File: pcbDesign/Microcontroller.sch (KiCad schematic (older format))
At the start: 7 parts

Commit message: Cerrected errors in the schematic and began work on the pcb layout
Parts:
- added C7: 500n, Capacitor_SMD:C_0402_1005Metric, symbol Device:C
- gave numbers to parts that had none: 7
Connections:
- net GND: now also C7.1
- net VBUS_3V3_CH0_REG: now also C7.2
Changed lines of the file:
@@
 $EndDescr
 $Comp
-L power:GND #PWR?
+L power:GND #PWR09
 U 1 1 6044DE61
 P 5300 5700
-F 0 "#PWR?" H 5300 5450 50  0001 C CNN
+F 0 "#PWR09" H 5300 5450 50  0001 C CNN
 F 1 "GND" H 5305 5527 50  0000 C CNN
 F 2 "" H 5300 5700 50  0001 C CNN
@@
 $EndComp
 $Comp
-L Device:R R?
+L Device:R R3
 U 1 1 6044DE67
 P 4400 5800
-F 0 "R?" V 4193 5800 50  0000 C CNN
+F 0 "R3" V 4193 5800 50  0000 C CNN
 F 1 "10K" V 4284 5800 50  0000 C CNN
 F 2 "Resistor_SMD:R_0402_1005Metric" V 4330 5800 50  0001 C CNN
@@
 P 4250 5450
 AR Path="/604550E7" Ref="C?"  Part="1"
-AR Path="/604479FD/604550E7" Ref="C?"  Part="1"
-F 0 "C?" H 4135 5404 50  0000 R CNN
+AR Path="/604479FD/604550E7" Ref="C5"  Part="1"
+F 0 "C5" H 4135 5404 50  0000 R CNN
 F 1 "1u" H 4135 5495 50  0000 R CNN
 F 2 "Capacitor_SMD:C_0402_1005Metric" H 4288 5300 50  0001 C CNN
@@
 $EndComp
 $Comp
-L power:GND #PWR?
+L power:GND #PWR07
 U 1 1 6045514C
 P 4100 5450
-F 0 "#PWR?" H 4100 5200 50  0001 C CNN
+F 0 "#PWR07" H 4100 5200 50  0001 C CNN
 F 1 "GND" H 4105 5277 50  0000 C CNN
 F 2 "" H 4100 5450 50  0001 C CNN
@@
 P 5300 3800
 AR Path="/6044DE5A" Ref="U?"  Part="1"
-AR Path="/604479FD/6044DE5A" Ref="U?"  Part="1"
-F 0 "U?" H 5300 1811 50  0001 C CNN
+AR Path="/604479FD/6044DE5A" Ref="U2"  Part="1"
+F 0 "U2" H 5300 1811 50  0001 C CNN
 F 1 "ATSAME51J18A-A" H 5300 1720 50  0000 C CNN
 F 2 "Package_QFP:TQFP-64_10x10mm_P0.5mm" H 6600 5700 50  0001 C CNN
@@
 P 5000 1750
 AR Path="/604A4817" Ref="C?"  Part="1"
-AR Path="/604479FD/604A4817" Ref="C?"  Part="1"
-F 0 "C?" H 4885 1704 50  0000 R CNN
+AR Path="/604479FD/604A4817" Ref="C6"  Part="1"
+F 0 "C6" H 4885 1704 50  0000 R CNN
 F 1 "1u" H 4885 1795 50  0000 R CNN
 F 2 "Capacitor_SMD:C_0402_1005Metric" H 5038 1600 50  0001 C CNN
@@
 $EndComp
 $Comp
-L power:GND #PWR?
+L power:GND #PWR08
 U 1 1 604A6978
 P 5000 1600
-F 0 "#PWR?" H 5000 1350 50  0001 C CNN
+F 0 "#PWR08" H 5000 1350 50  0001 C CNN
 F 1 "GND" H 5005 1427 50  0000 C CNN
 F 2 "" H 5000 1600 50  0001 C CNN
@@
 31
 $Comp
-L Device:Crystal Y?
+L Device:Crystal Y1
 U 1 1 604B1962
 P 3700 1950
-F 0 "Y?" H 3700 2218 50  0000 C CNN
+F 0 "Y1" H 3700 2218 50  0000 C CNN
 F 1 "32.768" H 3700 2127 50  0000 C CNN
 F 2 "Oscillator:Oscillator_SMD_Abracon_ASCO-4Pin_1.6x1.2mm" H 3700 1950 50  0001 C CNN
@@
 P 4000 1950
 AR Path="/604B399F" Ref="C?"  Part="1"
-AR Path="/604479FD/604B399F" Ref="C?"  Part="1"
-F 0 "C?" H 3885 1904 50  0000 R CNN
+AR Path="/604479FD/604B399F" Ref="C4"  Part="1"
+F 0 "C4" H 3885 1904 50  0000 R CNN
 F 1 "22u" H 3885 1995 50  0000 R CNN
 F 2 "Capacitor_SMD:C_0402_1005Metric" H 4038 1800 50  0001 C CNN
@@
 P 3400 1950
 AR Path="/604B6163" Ref="C?"  Part="1"
-AR Path="/604479FD/604B6163" Ref="C?"  Part="1"
-F 0 "C?" H 3285 1904 50  0000 R CNN
+AR Path="/604479FD/604B6163" Ref="C3"  Part="1"
+F 0 "C3" H 3285 1904 50  0000 R CNN
 F 1 "22u" H 3285 1995 50  0000 R CNN
 F 2 "Capacitor_SMD:C_0402_1005Metric" H 3438 1800 50  0001 C CNN
@@
 	3250 1600 3250 1950
 $Comp
-L power:GND #PWR?
+L power:GND #PWR06
 U 1 1 604B7059
 P 3700 1600
-F 0 "#PWR?" H 3700 1350 50  0001 C CNN
+F 0 "#PWR06" H 3700 1350 50  0001 C CNN
 F 1 "GND" H 3705 1427 50  0000 C CNN
 F 2 "" H 3700 1600 50  0001 C CNN
@@
 Text GLabel 4400 5000 0    50   BiDi ~ 0
 CAN_S
+$Comp
+L Device:C C?
+U 1 1 606356DA
+P 5500 1750
+AR Path="/606356DA" Ref="C?"  Part="1"
+AR Path="/604479FD/606356DA" Ref="C7"  Part="1"
+F 0 "C7" H 5385 1704 50  0000 R CNN
+F 1 "500n" H 5385 1795 50  0000 R CNN
+F 2 "Capacitor_SMD:C_0402_1005Metric" H 5538 1600 50  0001 C CNN
+F 3 "~" H 5500 1750 50  0001 C CNN
+	1    5500 1750
+	1    0    0    -1
+$EndComp
+$Comp
+L power:GND #PWR010
+U 1 1 6063675F
+P 5500 1600
+F 0 "#PWR010" H 5500 1350 50  0001 C CNN
+F 1 "GND" H 5505 1427 50  0000 C CNN
+F 2 "" H 5500 1600 50  0001 C CNN
+F 3 "" H 5500 1600 50  0001 C CNN
+	1    5500 1600
+	-1   0    0    1
+$EndComp
 $EndSCHEMATC

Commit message: Finnished routing
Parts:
- Y1: footprint Oscillator:Oscillator_SMD_Abracon_ASCO-4Pin_1.6x1.2mm -> Crystal:Crystal_SMD_2012-2Pin_2.0x1.2mm
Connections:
- net LED_PIN is gone; now on net 13: U2.60 (PB31/I15/S5.0/P0.1)
- net 13: no longer U2.26 (PB13/I13/S4.1/I2SMCK1/SD0WP/T27/P4.1/CRX1)
- net 15[I2SFS] renamed 7[I2SWS]
- net 6[I2SCK] renamed 6[I2SSCK]
- net USB_DM renamed USB_N
- net USB_DP renamed USB_P
- new net 15: U2.26 (PB13/I13/S4.1/I2SMCK1/SD0WP/T27/P4.1/CRX1)
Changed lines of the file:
@@
 $EndComp
 Text GLabel 4400 4800 0    50   BiDi ~ 0
-USB_DM
+USB_N
 Text GLabel 4400 4900 0    50   BiDi ~ 0
-USB_DP
+USB_P
 Wire Wire Line
 	4400 5400 4400 5450
@@
 AREF
 Text GLabel 8500 4000 2    50   BiDi ~ 0
-6[I2SCK]
+6[I2SSCK]
 Text GLabel 8500 4100 2    50   BiDi ~ 0
 14[I2SMCLK]
@@
 10[I2SDO]
 Text GLabel 4400 4400 0    50   BiDi ~ 0
-15[I2SFS]
+7[I2SWS]
 Text GLabel 3950 5650 0    50   BiDi ~ 0
 RST
@@
 Text GLabel 8500 3600 2    50   BiDi ~ 0
 12
-Text GLabel 8500 3700 2    50   BiDi ~ 0
+Text GLabel 8500 4600 3    50   BiDi ~ 0
 13
 Text GLabel 4400 2800 0    50   BiDi ~ 0
@@
 F 0 "Y1" H 3700 2218 50  0000 C CNN
 F 1 "32.768" H 3700 2127 50  0000 C CNN
-F 2 "Oscillator:Oscillator_SMD_Abracon_ASCO-4Pin_1.6x1.2mm" H 3700 1950 50  0001 C CNN
+F 2 "Crystal:Crystal_SMD_2012-2Pin_2.0x1.2mm" H 3700 1950 50  0001 C CNN
 F 3 "~" H 3700 1950 50  0001 C CNN
 	1    3700 1950
@@
 	-1   0    0    1
 $EndComp
+Wire Wire Line
+	8500 4600 8500 4500
+Text GLabel 8500 3700 2    50   BiDi ~ 0
+15
 $EndSCHEMATC

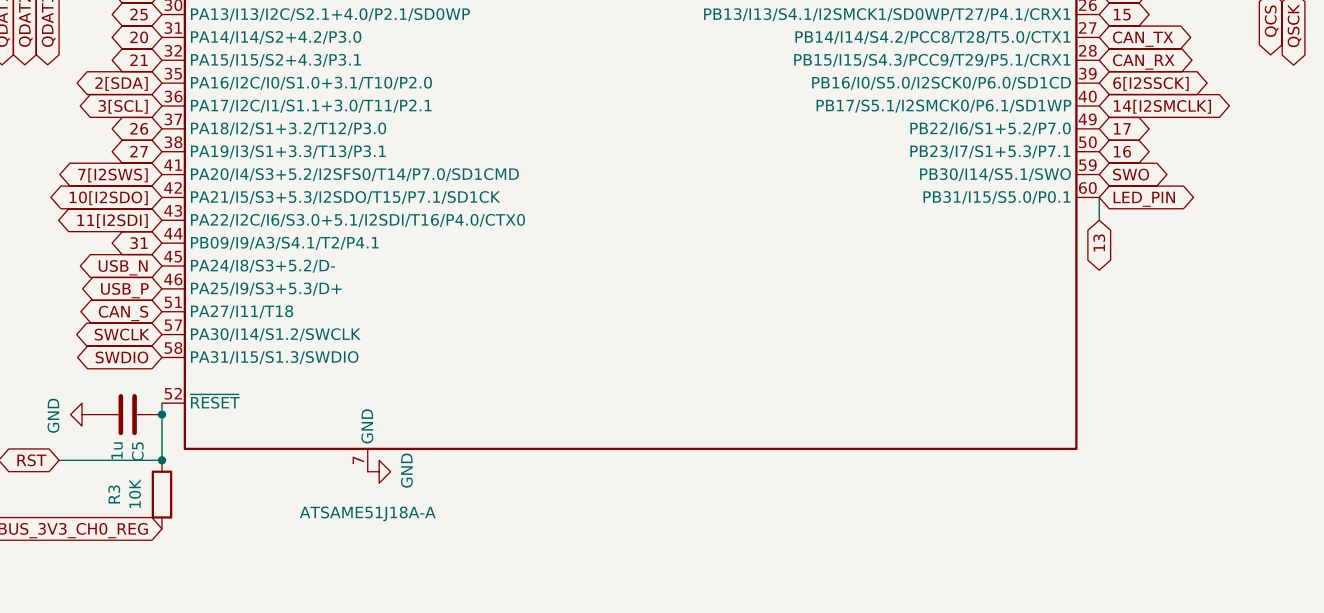
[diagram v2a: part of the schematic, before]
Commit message: Changed the layout of pins to make room for SWD and made the board longer
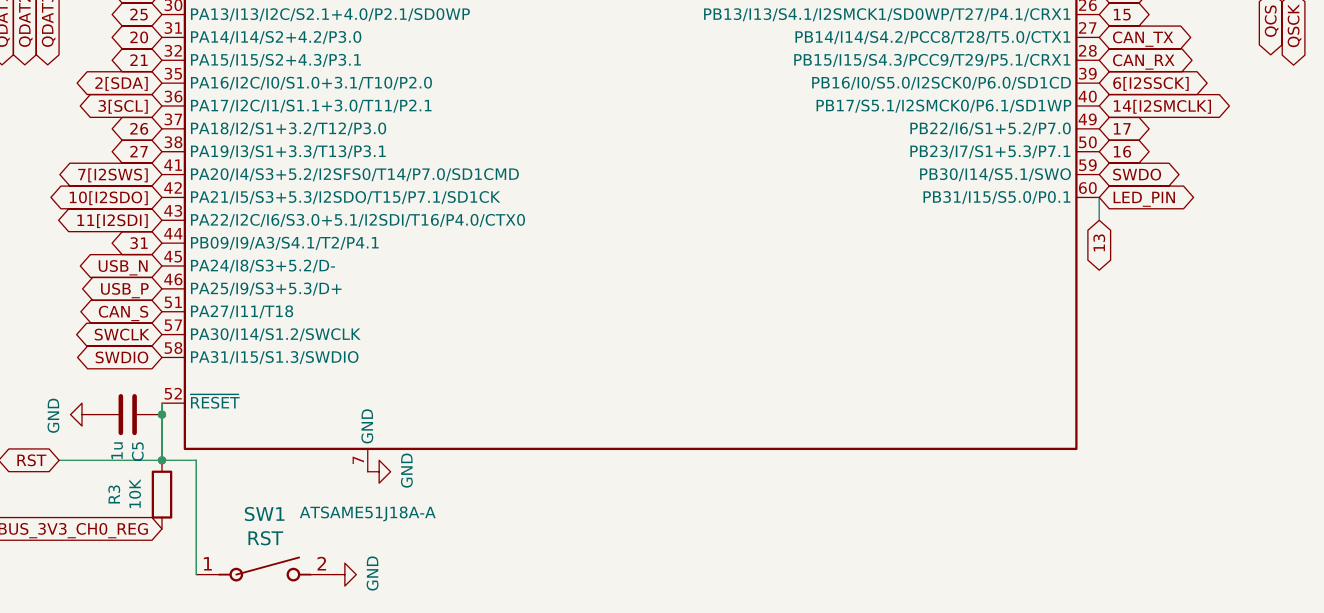
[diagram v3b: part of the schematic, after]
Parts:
- added SW1: RST, PTS636:PTS636 SM25F SMTR LFS, symbol PTS636:PTS636_SM25F_SMTR_LFS
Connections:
- net GND: now also SW1.2
- net RST: now also SW1.1
- net SWO renamed SWDO
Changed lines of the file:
@@
 SWDIO
 Text GLabel 8500 4400 2    50   BiDi ~ 0
-SWO
+SWDO
 Text GLabel 3600 3550 3    50   BiDi ~ 0
 QDAT0
@@
 Text GLabel 8500 3700 2    50   BiDi ~ 0
 15
+Wire Wire Line
+	4400 5650 4550 5650
+Wire Wire Line
+	4550 5650 4550 6150
+$Comp
+L power:GND #PWR0107
+U 1 1 60510F6A
+P 5150 6150
+F 0 "#PWR0107" H 5150 5900 50  0001 C CNN
+F 1 "GND" H 5155 5977 50  0000 C CNN
+F 2 "" H 5150 6150 50  0001 C CNN
+F 3 "" H 5150 6150 50  0001 C CNN
+	1    5150 6150
+	0    -1   -1   0
+$EndComp
+$Comp
+L PTS636:PTS636_SM25F_SMTR_LFS SW1
+U 1 1 60513314
+P 4850 6150
+F 0 "SW1" H 4850 6413 60  0000 C CNN
+F 1 "RST" H 4850 6307 60  0000 C CNN
+F 2 "PTS636:PTS636 SM25F SMTR LFS" H 4850 5965 60  0001 C CNN
+F 3 "" H 4850 6150 60  0000 C CNN
+	1    4850 6150
+	1    0    0    -1
+$EndComp
 $EndSCHEMATC

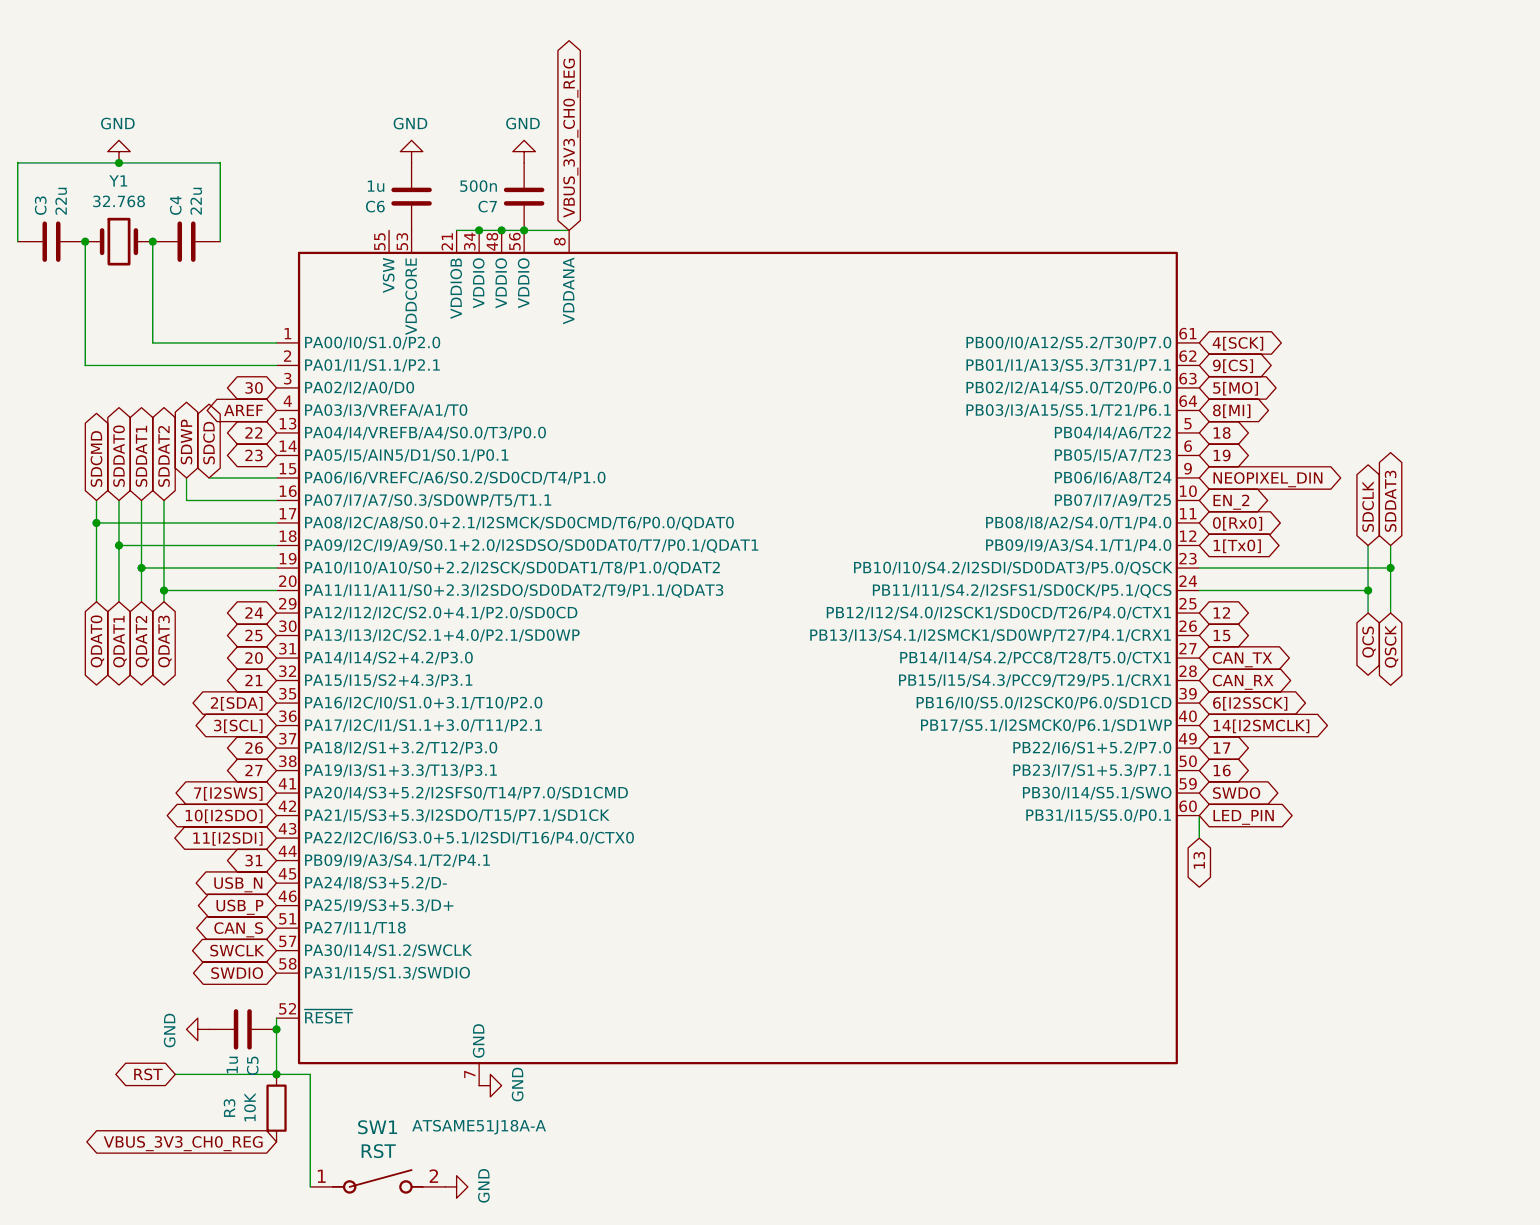
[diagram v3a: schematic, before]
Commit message: Rewired SD card to SPI for ease of use
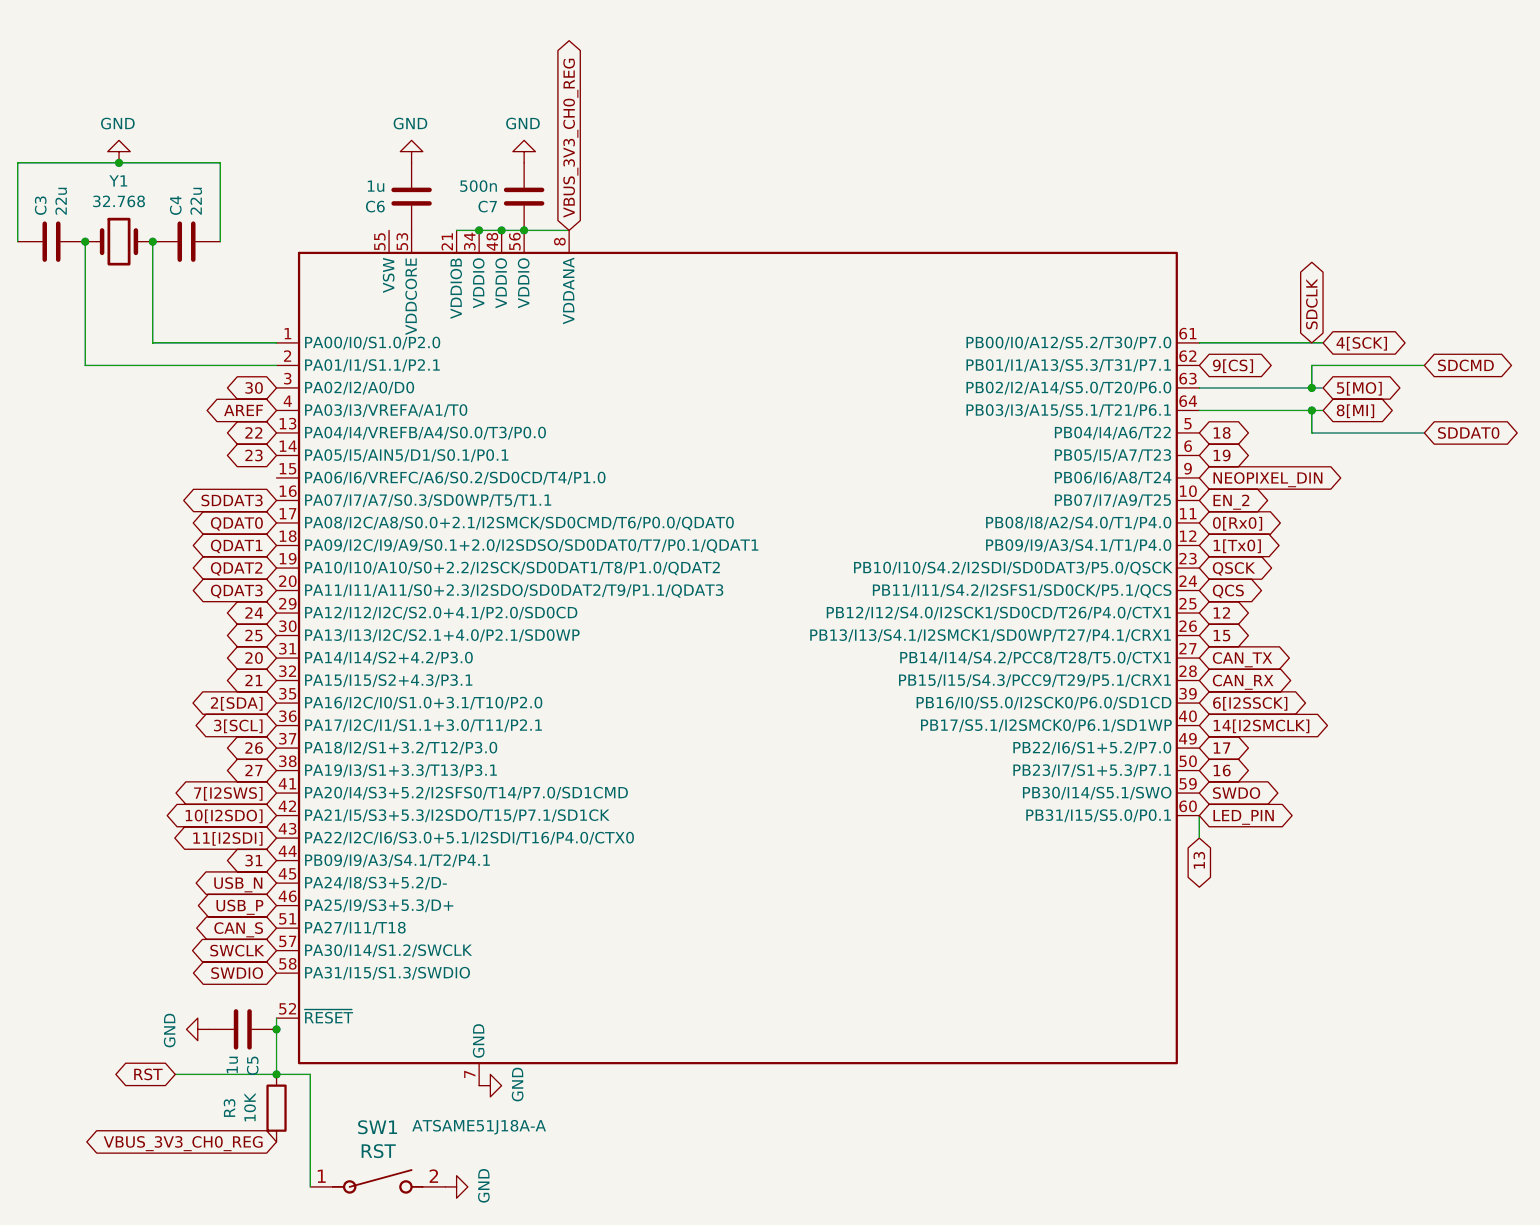
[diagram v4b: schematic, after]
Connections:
- net SDCD: no longer names the net of U2.15 (PA06/I6/VREFC/A6/S0.2/SD0CD/T4/P1.0)
- net SDWP renamed SDDAT3
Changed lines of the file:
@@
 Text GLabel 8500 4400 2    50   BiDi ~ 0
 SWDO
-Text GLabel 3600 3550 3    50   BiDi ~ 0
+Text GLabel 4400 3200 0    50   BiDi ~ 0
 QDAT0
-Text GLabel 3700 3550 3    50   BiDi ~ 0
+Text GLabel 4400 3300 0    50   BiDi ~ 0
 QDAT1
-Text GLabel 3800 3550 3    50   BiDi ~ 0
+Text GLabel 4400 3400 0    50   BiDi ~ 0
 QDAT2
-Text GLabel 3900 3550 3    50   BiDi ~ 0
+Text GLabel 4400 3500 0    50   BiDi ~ 0
 QDAT3
-Text GLabel 9350 3600 3    50   BiDi ~ 0
+Text GLabel 8500 3400 2    50   BiDi ~ 0
 QSCK
-Text GLabel 9250 3600 3    50   BiDi ~ 0
+Text GLabel 8500 3500 2    50   BiDi ~ 0
 QCS
 Text GLabel 4400 4000 0    50   BiDi ~ 0
@@
 	3950 5650 4400 5650
 Connection ~ 4400 5650
-Text GLabel 8500 2400 2    50   BiDi ~ 0
+Text GLabel 9050 2400 2    50   BiDi ~ 0
 4[SCK]
-Text GLabel 8500 2600 2    50   BiDi ~ 0
+Text GLabel 9050 2600 2    50   BiDi ~ 0
 5[MO]
-Text GLabel 8500 2700 2    50   BiDi ~ 0
+Text GLabel 9050 2700 2    50   BiDi ~ 0
 8[MI]
 Text GLabel 8500 2500 2    50   BiDi ~ 0
 9[CS]
-Text GLabel 3600 3100 1    50   BiDi ~ 0
+Text GLabel 9500 2500 2    50   BiDi ~ 0
 SDCMD
-Text GLabel 9350 3300 1    50   BiDi ~ 0
+Text GLabel 4400 3100 0    50   BiDi ~ 0
 SDDAT3
-Text GLabel 3900 3100 1    50   BiDi ~ 0
-SDDAT2
-Text GLabel 9250 3300 1    50   BiDi ~ 0
+Text GLabel 9000 2400 1    50   BiDi ~ 0
 SDCLK
-Text GLabel 3700 3100 1    50   BiDi ~ 0
+Text GLabel 9500 2800 2    50   BiDi ~ 0
 SDDAT0
-Text GLabel 3800 3100 1    50   BiDi ~ 0
-SDDAT1
-Wire Wire Line
-	4400 3500 3900 3500
-Wire Wire Line
-	3900 3500 3900 3550
-Wire Wire Line
-	3800 3400 3800 3550
-Wire Wire Line
-	4400 3300 3700 3300
-Wire Wire Line
-	3700 3300 3700 3550
-Wire Wire Line
-	4400 3200 3600 3200
-Wire Wire Line
-	3600 3200 3600 3550
-Wire Wire Line
-	3600 3100 3600 3200
-Connection ~ 3600 3200
-Wire Wire Line
-	3700 3100 3700 3300
-Connection ~ 3700 3300
-Wire Wire Line
-	4400 3400 3800 3400
-Wire Wire Line
-	3800 3100 3800 3400
-Connection ~ 3800 3400
-Wire Wire Line
-	3900 3100 3900 3500
-Connection ~ 3900 3500
-Wire Wire Line
-	8500 3400 9350 3400
-Wire Wire Line
-	9350 3400 9350 3300
-Wire Wire Line
-	8500 3500 9250 3500
-Wire Wire Line
-	9250 3500 9250 3300
-Wire Wire Line
-	9350 3600 9350 3400
-Connection ~ 9350 3400
-Wire Wire Line
-	9250 3600 9250 3500
-Connection ~ 9250 3500
 Text GLabel 8500 2800 2    50   BiDi ~ 0
 18
@@
 Text GLabel 8500 4500 2    50   BiDi ~ 0
 LED_PIN
-Text GLabel 4100 3000 1    50   BiDi ~ 0
-SDCD
-Text GLabel 4000 3000 1    50   BiDi ~ 0
-SDWP
-Wire Wire Line
-	4100 3000 4400 3000
-Wire Wire Line
-	4400 3100 4000 3100
-Wire Wire Line
-	4000 3100 4000 3000
 Text GLabel 8500 3300 2    50   BiDi ~ 0
 1[Tx0]
@@
 	1    0    0    -1
 $EndComp
+Wire Wire Line
+	8500 2600 9000 2600
+Wire Wire Line
+	9050 2700 9000 2700
+Wire Wire Line
+	8500 2400 9050 2400
+Wire Wire Line
+	9500 2500 9000 2500
+Wire Wire Line
+	9000 2500 9000 2600
+Connection ~ 9000 2600
+Wire Wire Line
+	9000 2600 9050 2600
+Wire Wire Line
+	9500 2800 9000 2800
+Wire Wire Line
+	9000 2800 9000 2700
+Connection ~ 9000 2700
+Wire Wire Line
+	9000 2700 8500 2700
 $EndSCHEMATC

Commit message: Begun to make changes to the design
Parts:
- SW1: symbol PTS636:PTS636_SM25F_SMTR_LFS -> ATSAME51J18A-devboard-rescue:PTS636_SM25F_SMTR_LFS-PTS636
- U2: symbol MCU_Microchip_SAME:ATSAME51J18A-A -> ATSAME51J18A-devboard-rescue:ATSAME51J18A-A-MCU_Microchip_SAME
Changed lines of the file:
@@
 Connection ~ 5300 1900
 $Comp
-L MCU_Microchip_SAME:ATSAME51J18A-A U?
+L ATSAME51J18A-devboard-rescue:ATSAME51J18A-A-MCU_Microchip_SAME U?
 U 1 1 6044DE5A
 P 5300 3800
@@
 $EndComp
 $Comp
-L PTS636:PTS636_SM25F_SMTR_LFS SW1
+L ATSAME51J18A-devboard-rescue:PTS636_SM25F_SMTR_LFS-PTS636 SW1
 U 1 1 60513314
 P 4850 6150
